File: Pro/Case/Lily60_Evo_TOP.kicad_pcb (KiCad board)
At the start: 2 copper layers, 142.5 x 112.8 mm, 5 parts

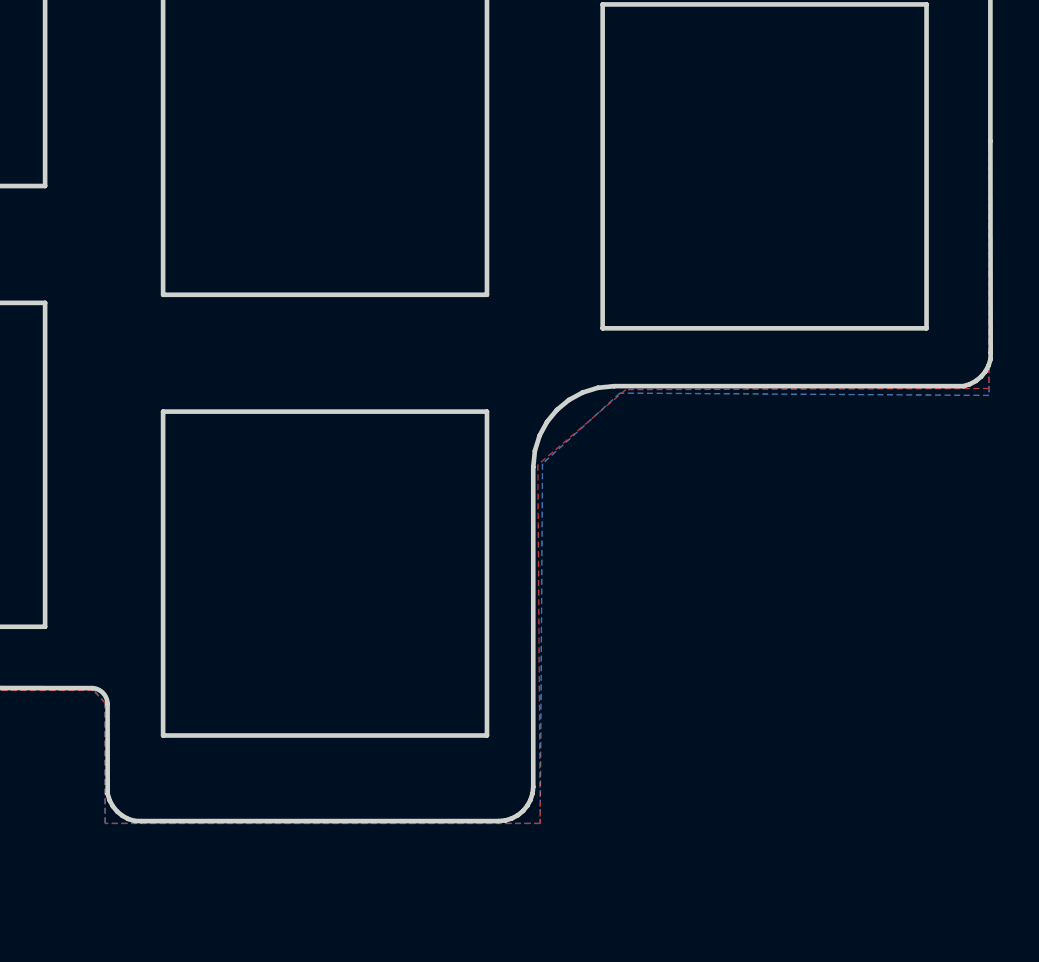
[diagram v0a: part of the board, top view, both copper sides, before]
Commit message: SW31 can be an encoder or a MW Switch
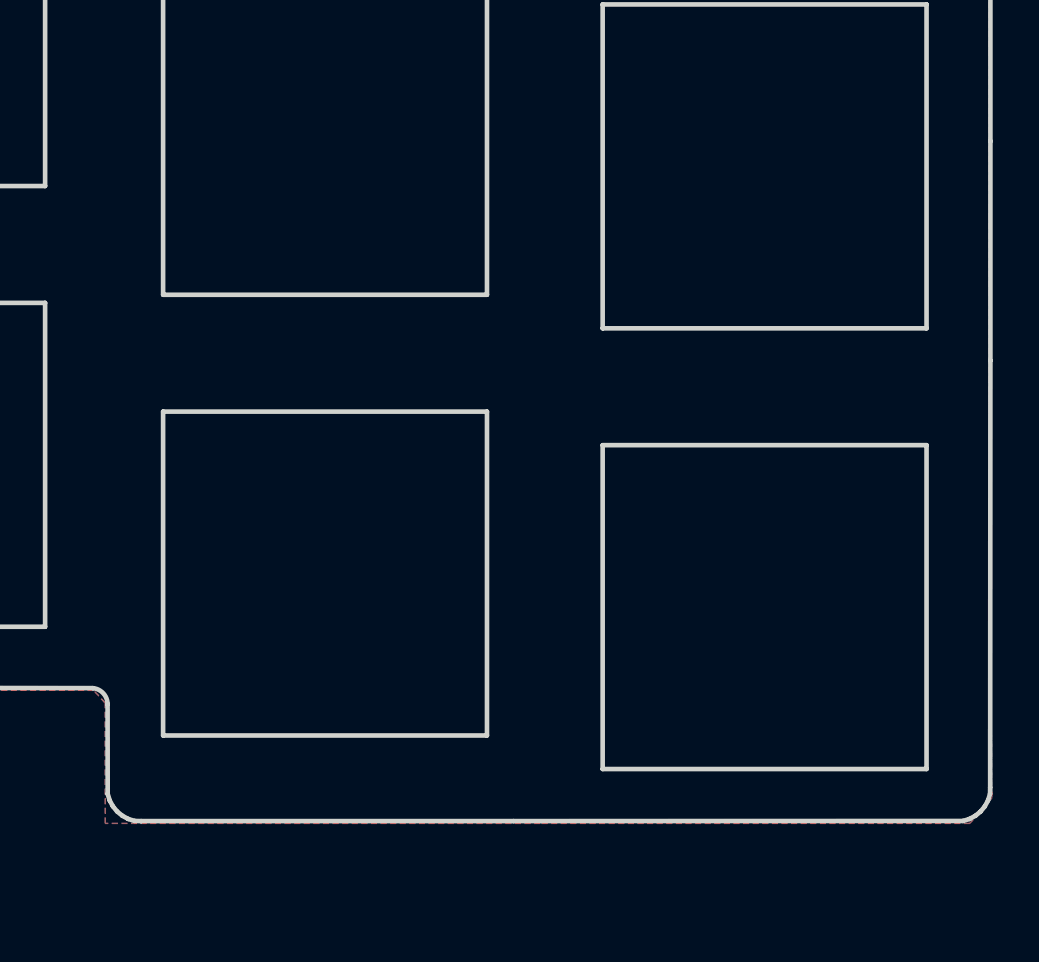
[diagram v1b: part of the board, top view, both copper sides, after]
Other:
- outline, holes or cut-outs redrawn
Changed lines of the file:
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@@
   (general
     (thickness 1.6)
-    (drawings 236)
+    (drawings 224)
     (tracks 0)
     (zones 0)
@@
     (pad "" thru_hole circle (at 0 0 90) (size 4 4) (drill 2.4) (layers *.Cu *.Mask))
   )
+  (gr_line (start 225.444553 138.027496) (end 225.357217 138.309152) (layer Edge.Cuts) (width 0.2))
+  (gr_line (start 225.219001 138.563961) (end 225.035913 138.785913) (layer Edge.Cuts) (width 0.2))
+  (gr_line (start 224.559152 139.107218) (end 224.277496 139.194553) (layer Edge.Cuts) (width 0.2))
+  (gr_line (start 225.45 137.75) (end 225.444553 138.027496) (layer Edge.Cuts) (width 0.2))
+  (gr_line (start 225.035913 138.785913) (end 224.81396 138.969002) (layer Edge.Cuts) (width 0.2))
+  (gr_line (start 224.81396 138.969002) (end 224.559152 139.107218) (layer Edge.Cuts) (width 0.2))
+  (gr_line (start 225.357217 138.309152) (end 225.219001 138.563961) (layer Edge.Cuts) (width 0.2))
+  (gr_line (start 204.85 139.2) (end 224.277496 139.194553) (layer Edge.Cuts) (width 0.2))
+  (gr_line (start 225.459999 119.289735) (end 225.45 137.75) (layer Edge.Cuts) (width 0.2))
+  (gr_line (start 208.7 122.95) (end 222.7 122.95) (layer Edge.Cuts) (width 0.2))
+  (gr_line (start 222.7 122.95) (end 222.7 136.95) (layer Edge.Cuts) (width 0.2))
+  (gr_line (start 222.7 136.95) (end 208.7 136.95) (layer Edge.Cuts) (width 0.2))
+  (gr_line (start 208.7 136.95) (end 208.7 122.95) (layer Edge.Cuts) (width 0.2))
   (gr_text JLCJLCJLCJLC (at 158.5 131.4) (layer F.SilkS)
     (effects (font (size 1 1) (thickness 0.2)))
   )
-  (gr_line (start 225.472504 118.955447) (end 225.467057 119.232943) (layer Edge.Cuts) (width 0.2))
-  (gr_line (start 225.467057 119.232943) (end 225.379721 119.514599) (layer Edge.Cuts) (width 0.2))
-  (gr_line (start 225.241505 119.769408) (end 225.058417 119.99136) (layer Edge.Cuts) (width 0.2))
-  (gr_line (start 225.058417 119.99136) (end 224.836464 120.174449) (layer Edge.Cuts) (width 0.2))
-  (gr_line (start 225.379721 119.514599) (end 225.241505 119.769408) (layer Edge.Cuts) (width 0.2))
-  (gr_line (start 224.836464 120.174449) (end 224.581656 120.312665) (layer Edge.Cuts) (width 0.2))
-  (gr_line (start 224.581656 120.312665) (end 224.3 120.4) (layer Edge.Cuts) (width 0.2))
-  (gr_line (start 209.2 120.4) (end 224.3 120.4) (layer Edge.Cuts) (width 0.2))
-  (gr_line (start 205.7 123.9) (end 205.771043 123.194176) (layer Edge.Cuts) (width 0.2))
-  (gr_line (start 207.242425 120.99733) (end 207.836978 120.674826) (layer Edge.Cuts) (width 0.2))
-  (gr_line (start 205.771043 123.194176) (end 205.974826 122.536978) (layer Edge.Cuts) (width 0.2))
-  (gr_line (start 208.494176 120.471043) (end 209.2 120.4) (layer Edge.Cuts) (width 0.2))
-  (gr_line (start 205.974826 122.536978) (end 206.29733 121.942425) (layer Edge.Cuts) (width 0.2))
-  (gr_line (start 206.724536 121.424536) (end 207.242425 120.99733) (layer Edge.Cuts) (width 0.2))
-  (gr_line (start 207.836978 120.674826) (end 208.494176 120.471043) (layer Edge.Cuts) (width 0.2))
-  (gr_line (start 206.29733 121.942425) (end 206.724536 121.424536) (layer Edge.Cuts) (width 0.2))
-  (gr_line (start 205.260913 138.760913) (end 205.038961 138.944001) (layer Edge.Cuts) (width 0.2))
-  (gr_line (start 205.7 137.722394) (end 205.669553 138.002496) (layer Edge.Cuts) (width 0.2))
-  (gr_line (start 205.669553 138.002496) (end 205.582217 138.284152) (layer Edge.Cuts) (width 0.2))
-  (gr_line (start 205.444001 138.53896) (end 205.260913 138.760913) (layer Edge.Cuts) (width 0.2))
-  (gr_line (start 205.582217 138.284152) (end 205.444001 138.53896) (layer Edge.Cuts) (width 0.2))
-  (gr_line (start 205.038961 138.944001) (end 204.784152 139.082217) (layer Edge.Cuts) (width 0.2))
-  (gr_line (start 204.784152 139.082217) (end 204.502496 139.169553) (layer Edge.Cuts) (width 0.2))
-  (gr_line (start 205.7 123.9) (end 205.7 137.722394) (layer Edge.Cuts) (width 0.2))
-  (gr_line (start 204.502496 139.169553) (end 204.2 139.2) (layer Edge.Cuts) (width 0.2))
   (gr_line (start 106.24175 142.715431) (end 99.241752 130.591074) (layer Edge.Cuts) (width 0.2))
   (gr_line (start 118.366106 135.715431) (end 106.24175 142.715431) (layer Edge.Cuts) (width 0.2))
@@
   (gr_line (start 147.9 133.4) (end 186.658574 133.452455) (layer Edge.Cuts) (width 0.2))
   (gr_line (start 109.882452 148.801617) (end 113.554472 146.663782) (layer Edge.Cuts) (width 0.2))
-  (gr_line (start 188.75 139.2) (end 204.2 139.2) (layer Edge.Cuts) (width 0.2))
+  (gr_line (start 188.75 139.2) (end 204.85 139.2) (layer Edge.Cuts) (width 0.2))
   (gr_line (start 115.211711 37.086762) (end 112.93 37.09) (layer Edge.Cuts) (width 0.2))
   (gr_line (start 199.807654 38.170488) (end 189.919538 37.585374) (layer Edge.Cuts) (width 0.2))
@@
   (gr_line (start 224.278471 42.15619) (end 220.889319 40.963847) (layer Edge.Cuts) (width 0.2))
   (gr_line (start 225.46 43.436755) (end 224.278471 42.15619) (layer Edge.Cuts) (width 0.2))
-  (gr_line (start 225.46 109.808112) (end 225.472504 118.955447) (layer Edge.Cuts) (width 0.2))
+  (gr_line (start 225.46 109.808112) (end 225.459999 119.289735) (layer Edge.Cuts) (width 0.2))
   (gr_line (start 225.46 100.32649) (end 225.46 109.808112) (layer Edge.Cuts) (width 0.2))
   (gr_line (start 225.46 90.844867) (end 225.46 100.32649) (layer Edge.Cuts) (width 0.2))
@@
       (pts
         (xy 82.89 87.24) (xy 108.55 87.32) (xy 110.75 84.57) (xy 110.34 37.01) (xy 225.4 37)
-        (xy 225.4 120.5) (xy 209.7 120.55) (xy 205.9 123.8) (xy 206 139.3) (xy 187.2 139.3)
+        (xy 225.4 120.5) (xy 225.525 138.2) (xy 224.575 139.3) (xy 206 139.3) (xy 187.2 139.3)
         (xy 187.2 134.1) (xy 186.7 133.55) (xy 147.95 133.5) (xy 127.15 139.05) (xy 107.55 150.25)
         (xy 90 119.6) (xy 83.62 104.75)
@@
       (pts
         (xy 82.91 87.25) (xy 108.55 87.29) (xy 110.75 84.58) (xy 110.37 37) (xy 225.4 37)
-        (xy 225.4 120.8) (xy 209.45 120.7) (xy 206.1 123.75) (xy 206 139.3) (xy 187.2 139.3)
+        (xy 225.4 120.8) (xy 225.525 138.2) (xy 224.575 139.3) (xy 206 139.3) (xy 187.2 139.3)
         (xy 187.2 134.1) (xy 186.7 133.55) (xy 148 133.5) (xy 127.15 139.05) (xy 107.55 150.25)
         (xy 90 120) (xy 83.58 104.79)
@@
       )
     )
+  )
+  (zone (net 0) (net_name "") (layers F&B.Cu) (hatch edge 0.508)
+    (connect_pads (clearance 0.508))
+    (min_thickness 0.254)
+    (keepout (tracks not_allowed) (vias not_allowed) (copperpour not_allowed))
+    (fill (arc_segments 16) (thermal_gap 0.508) (thermal_bridge_width 0.508))
+    (polygon
+      (pts
+        (xy 208.7 122.95) (xy 222.7 122.95) (xy 222.7 136.95) (xy 208.71 136.95)
+      )
+    )
